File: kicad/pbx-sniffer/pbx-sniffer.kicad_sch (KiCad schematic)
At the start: 7 parts, among them J49 USB_C_Receptacle_USB2.0_14P, U1 STM32H523CCUx, U2 AZ1117CH2-3.3

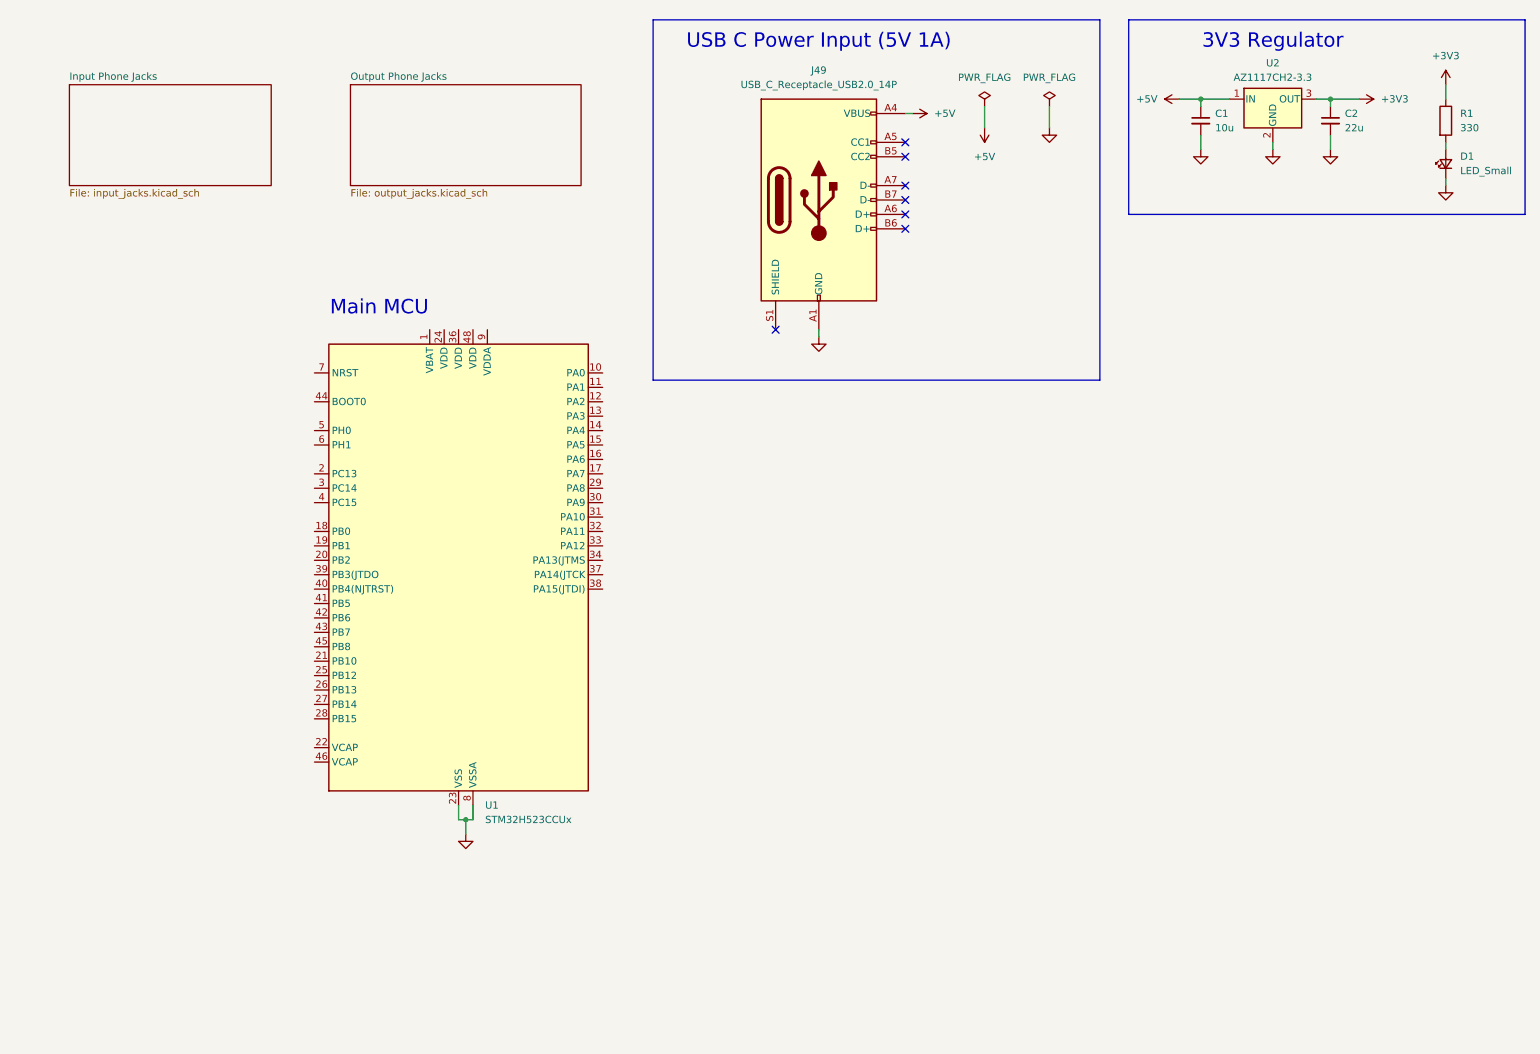
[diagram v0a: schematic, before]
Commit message: picked new MCU and updated some part numbers
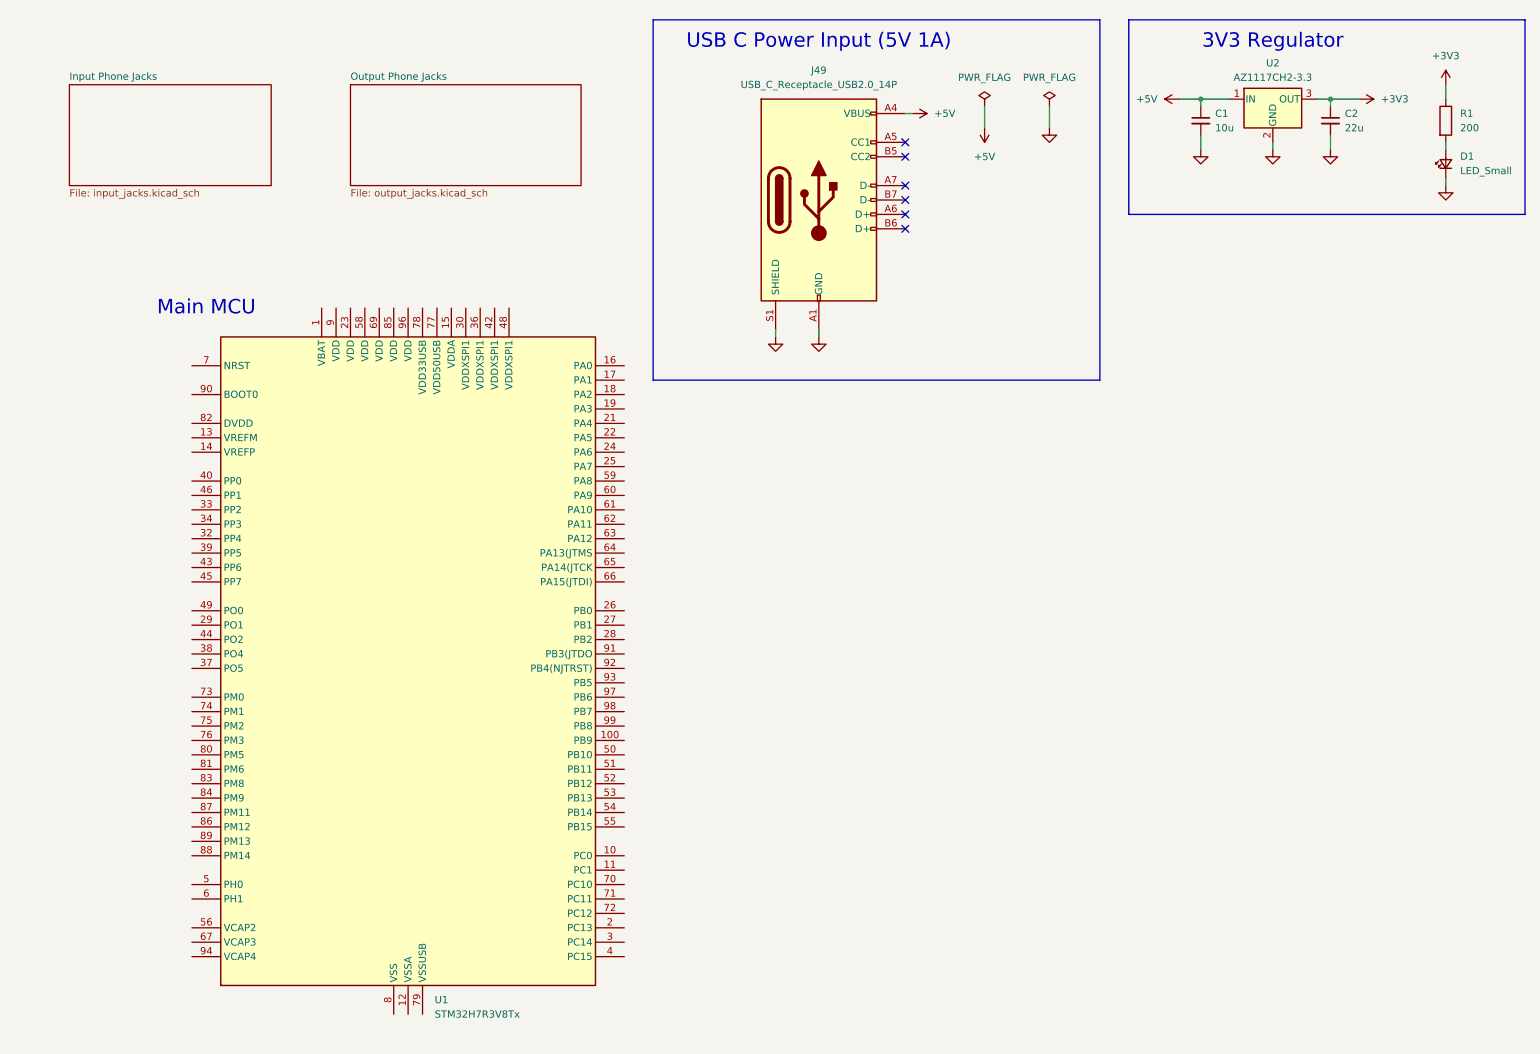
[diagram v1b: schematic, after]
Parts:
- removed U1: STM32H523CCUx, Package_DFN_QFN:QFN-48-1EP_7x7mm_P0.5mm_EP5.6x5.6mm, symbol MCU_ST_STM32H5:STM32H523CCUx
- added U1: STM32H7R3V8Tx, Package_QFP:LQFP-100_14x14mm_P0.5mm, symbol MCU_ST_STM32H7:STM32H7R3V8Tx
- C1: footprint (none) -> Capacitor_SMD:C_0603_1608Metric; DKPN (none) -> 1276-1192-1-ND
- C2: footprint (none) -> Capacitor_SMD:C_0603_1608Metric; DKPN (none) -> 1276-1274-1-ND
- D1: footprint (none) -> LED_SMD:LED_0805_2012Metric; DKPN (none) -> 160-1426-1-ND
- J49: footprint (none) -> Connector_USB:USB_C_Receptacle_GCT_USB4125-xx-x_6P_TopMnt_Horizontal; DKPN (none) -> 2073-USB4125-GF-ACT-ND
- R1: value 330 -> 200; footprint (none) -> Resistor_SMD:R_0402_1005Metric; DKPN (none) -> 311-200LRCT-ND
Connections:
- net GND: now also J49.S1 (SHIELD)
- new net: U1.20 (VSS), U1.31 (VSS), U1.35 (VSS), U1.41 (VSS), U1.47 (VSS), U1.57 (VSS), U1.68 (VSS), U1.8 (VSS), U1.95 (VSS)
- no-connect marks 7 -> 6

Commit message: add external power circuitry for mcu
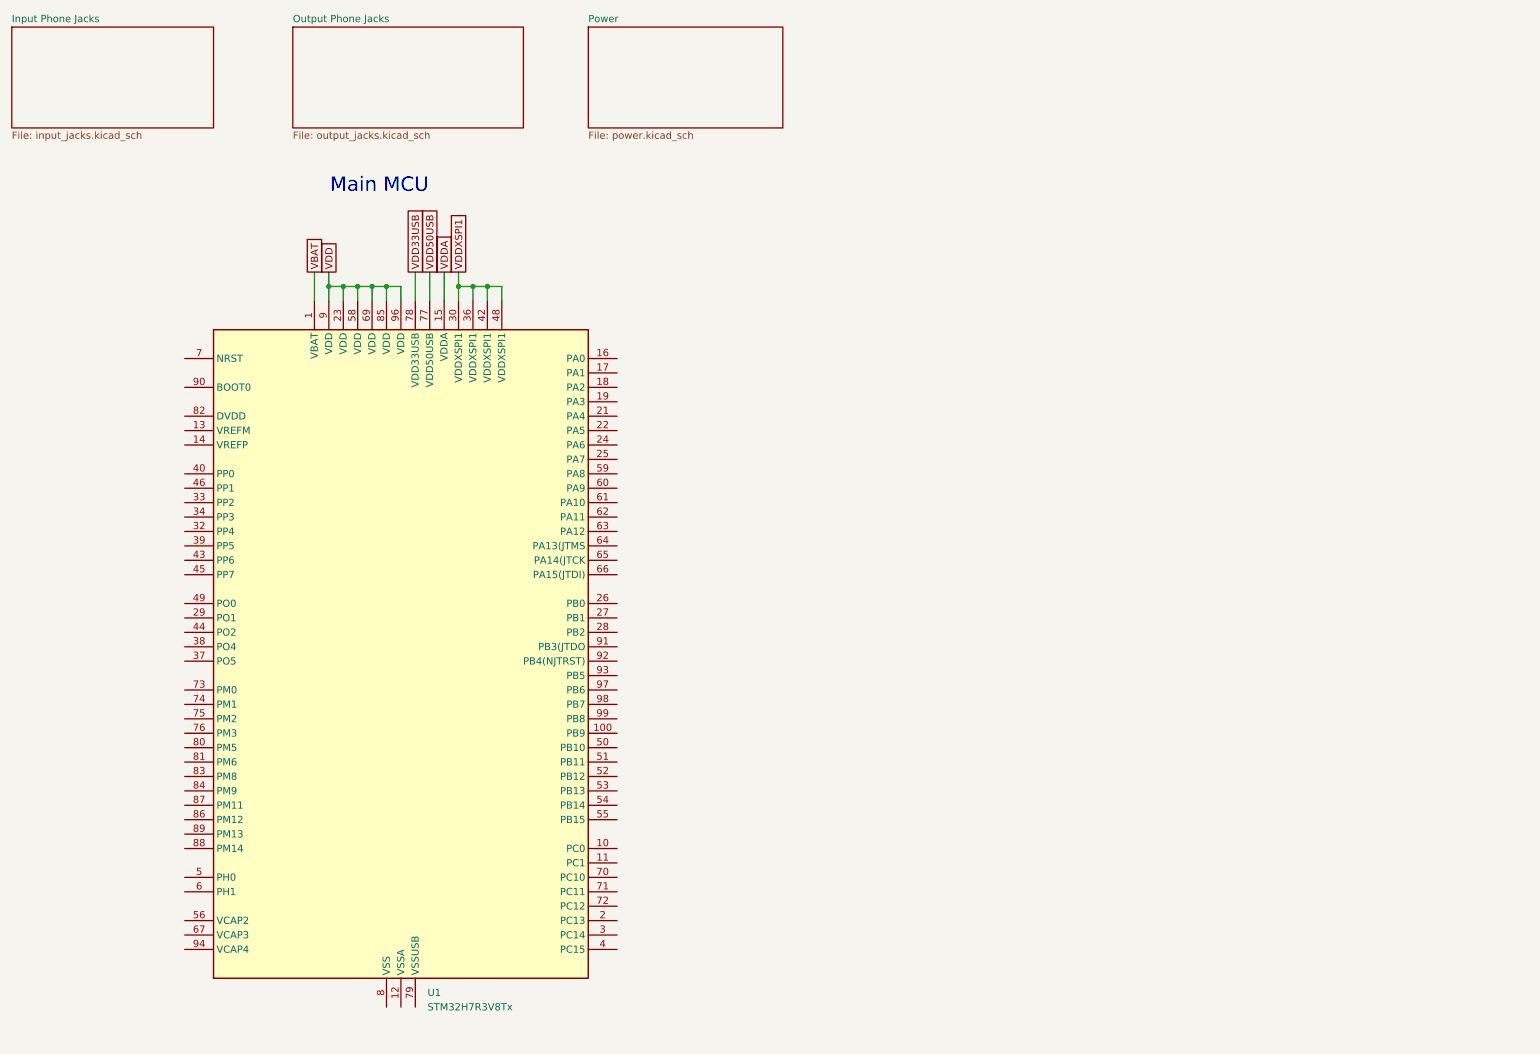
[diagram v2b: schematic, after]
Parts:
- removed C1: 10u, Capacitor_SMD:C_0603_1608Metric, symbol Device:C_Small
- removed C2: 22u, Capacitor_SMD:C_0603_1608Metric, symbol Device:C_Small
- removed D1: LED_Small, LED_SMD:LED_0805_2012Metric, symbol Device:LED_Small
- removed J49: USB_C_Receptacle_USB2.0_14P, Connector_USB:USB_C_Receptacle_GCT_USB4125-xx-x_6P_TopMnt_Horizontal, symbol Connector:USB_C_Receptacle_USB2.0_14P
- removed R1: 200, Resistor_SMD:R_0402_1005Metric, symbol Device:R
- removed U2: AZ1117CH2-3.3, Package_TO_SOT_SMD:TO-252-2, symbol Regulator_Linear:AZ1117CH2-3.3
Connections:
- net VBAT: now reaches U1.1 (VBAT)
- net VDDA: now reaches U1.15 (VDDA)
- net VDD: now reaches U1.23 (VDD)
- net VDD: now also U1.58 (VDD), U1.69 (VDD), U1.85 (VDD), U1.9 (VDD), U1.96 (VDD)
- net VDDXSPI1: now reaches U1.30 (VDDXSPI1)
- net VDDXSPI1: now also U1.36 (VDDXSPI1), U1.42 (VDDXSPI1), U1.48 (VDDXSPI1)
- net VDD50USB: now reaches U1.77 (VDD50USB)
- net VDD33USB: now reaches U1.78 (VDD33USB)
- no-connect marks 6 -> 0
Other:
- added sheet Power (power.kicad_sch)
- note removed: "3V3 Regulator"
- note removed: "USB C Power Input (5V 1A)"
- moved on the sheet: U1

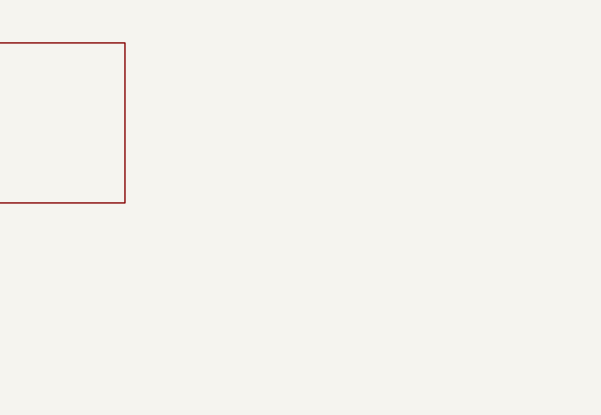
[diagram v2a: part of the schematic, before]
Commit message: drew schematic of naive wiretap circuit
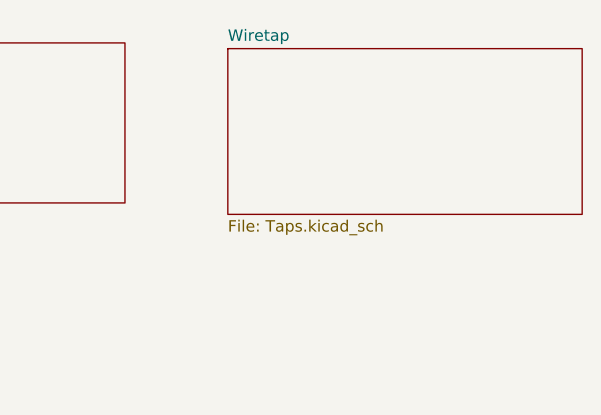
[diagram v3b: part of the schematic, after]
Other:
- added sheet Wiretap (Taps.kicad_sch)

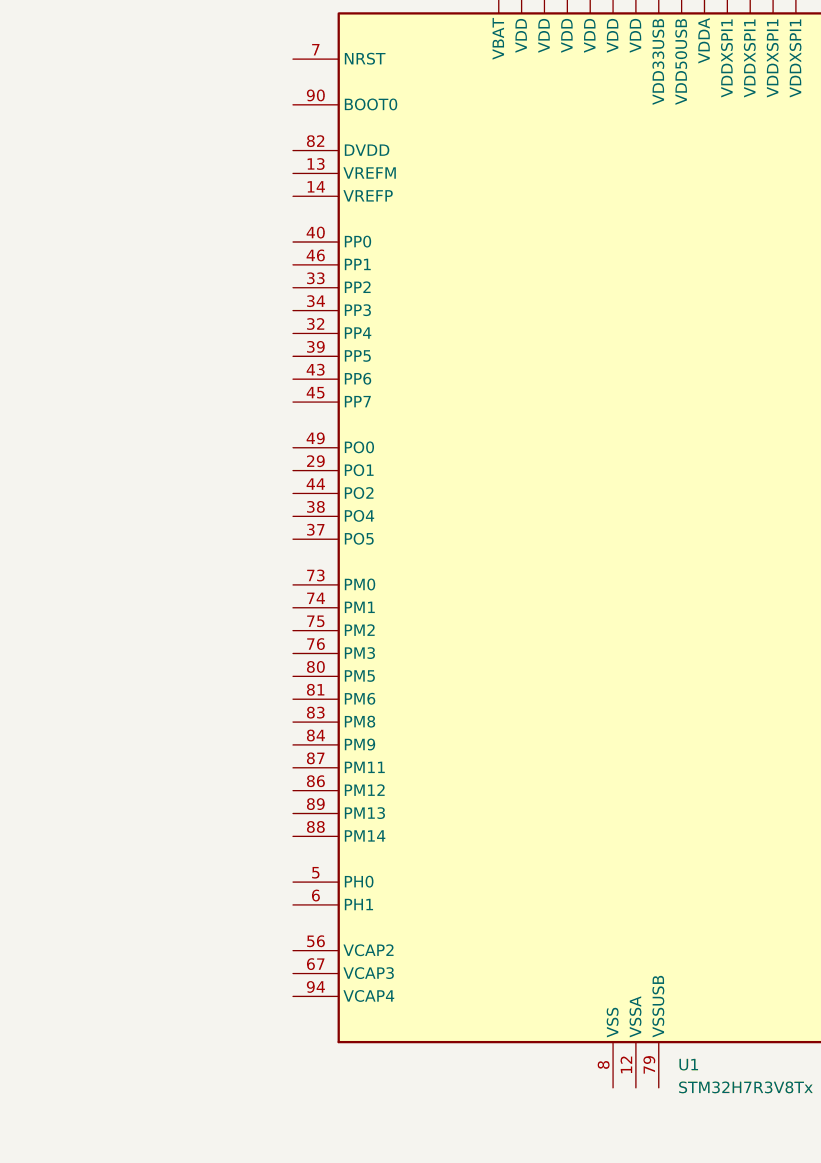
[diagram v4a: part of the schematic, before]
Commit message: add more supporting external circuitry for the MCU
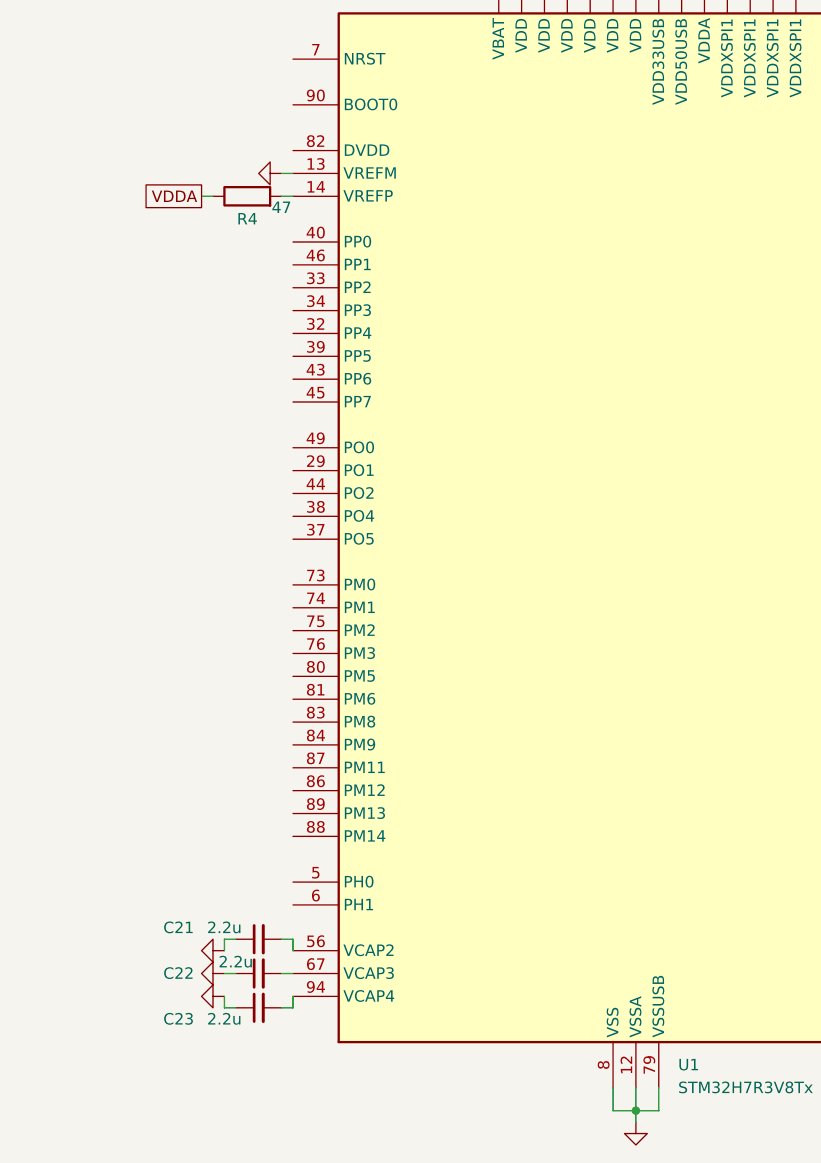
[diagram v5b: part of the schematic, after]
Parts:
- added C21, C22, C23: 2.2u, symbol Device:C_Small
- added R4: 47, symbol Device:R
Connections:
- net VDDA: now also R4.1
- net GND: now reaches U1.12 (VSSA)
- net GND: now also U1.13 (VREFM), U1.20 (VSS), U1.31 (VSS), U1.35 (VSS), U1.41 (VSS), U1.47 (VSS), U1.57 (VSS), U1.68 (VSS), U1.79 (VSSUSB), U1.8 (VSS), U1.95 (VSS), C21.1, C22.1, C23.1
- net at U1.14 (VREFP): now also R4.2
- net at U1.56 (VCAP2): now also C21.2
- net at U1.67 (VCAP3): now also C22.2
- net at U1.94 (VCAP4): now also C23.2

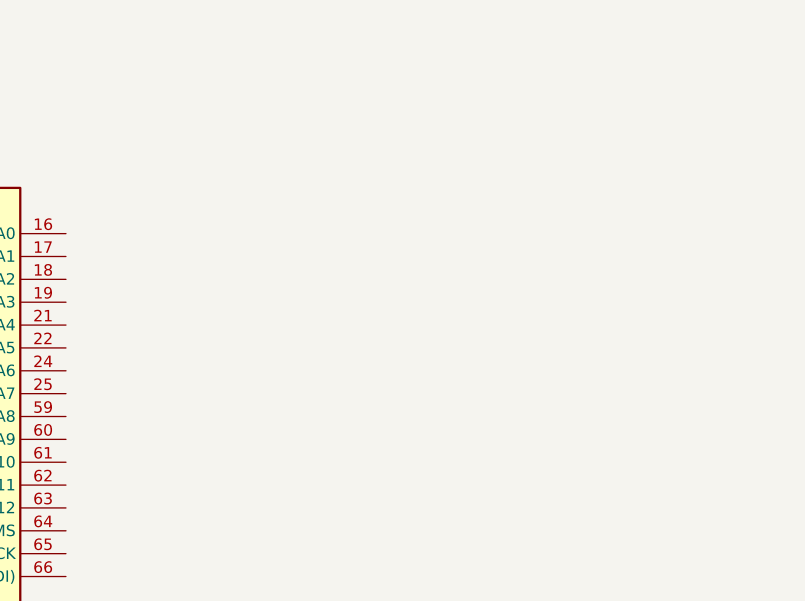
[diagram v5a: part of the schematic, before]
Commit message: add external flash chip
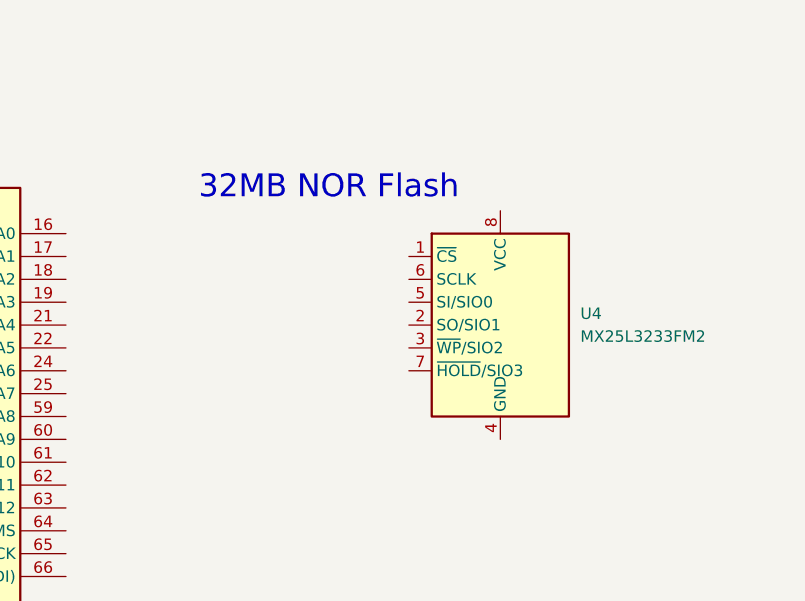
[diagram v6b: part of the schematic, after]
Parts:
- added U4: MX25L3233FM2, Package_SO:SOIC-8_5.3x5.3mm_P1.27mm, symbol Memory_Flash:MX25L3233FM2
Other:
- note added: "32MB NOR Flash"

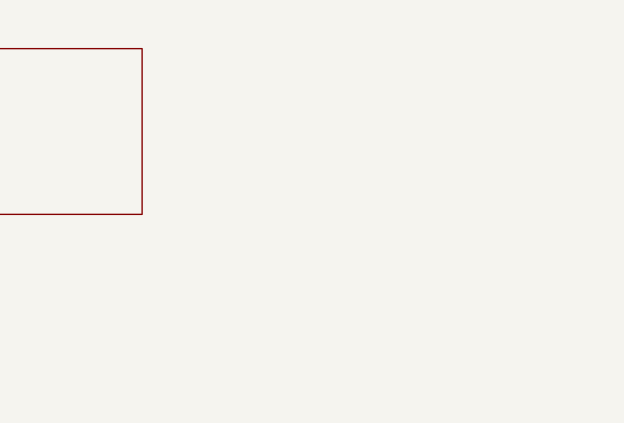
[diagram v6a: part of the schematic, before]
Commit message: added relays and wiretap circuits to schematic
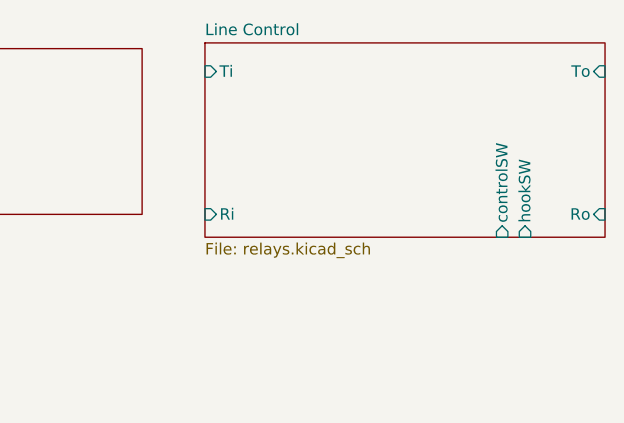
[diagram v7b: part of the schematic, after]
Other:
- added sheet Line Control (relays.kicad_sch)
